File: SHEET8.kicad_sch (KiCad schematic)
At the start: 27 parts, among them J6 CASSETTE, K1 DIP_RELAY, P3 CONN_4, P4 4_PIN_BERG_2X2_STRIP, U1 MC1741, U26 74LS175, U34 8253-5, U63 74LS38, U67 74LS74, U95 75477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

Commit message: Fixed LS and S parts
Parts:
- R10: value 33 -> 33 1/2W
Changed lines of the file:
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@@
 			)
 		)
-		(property "Value" "33"
+		(property "Value" "33 1/2W"
 			(at 316.23 104.14 0)
 			(effects

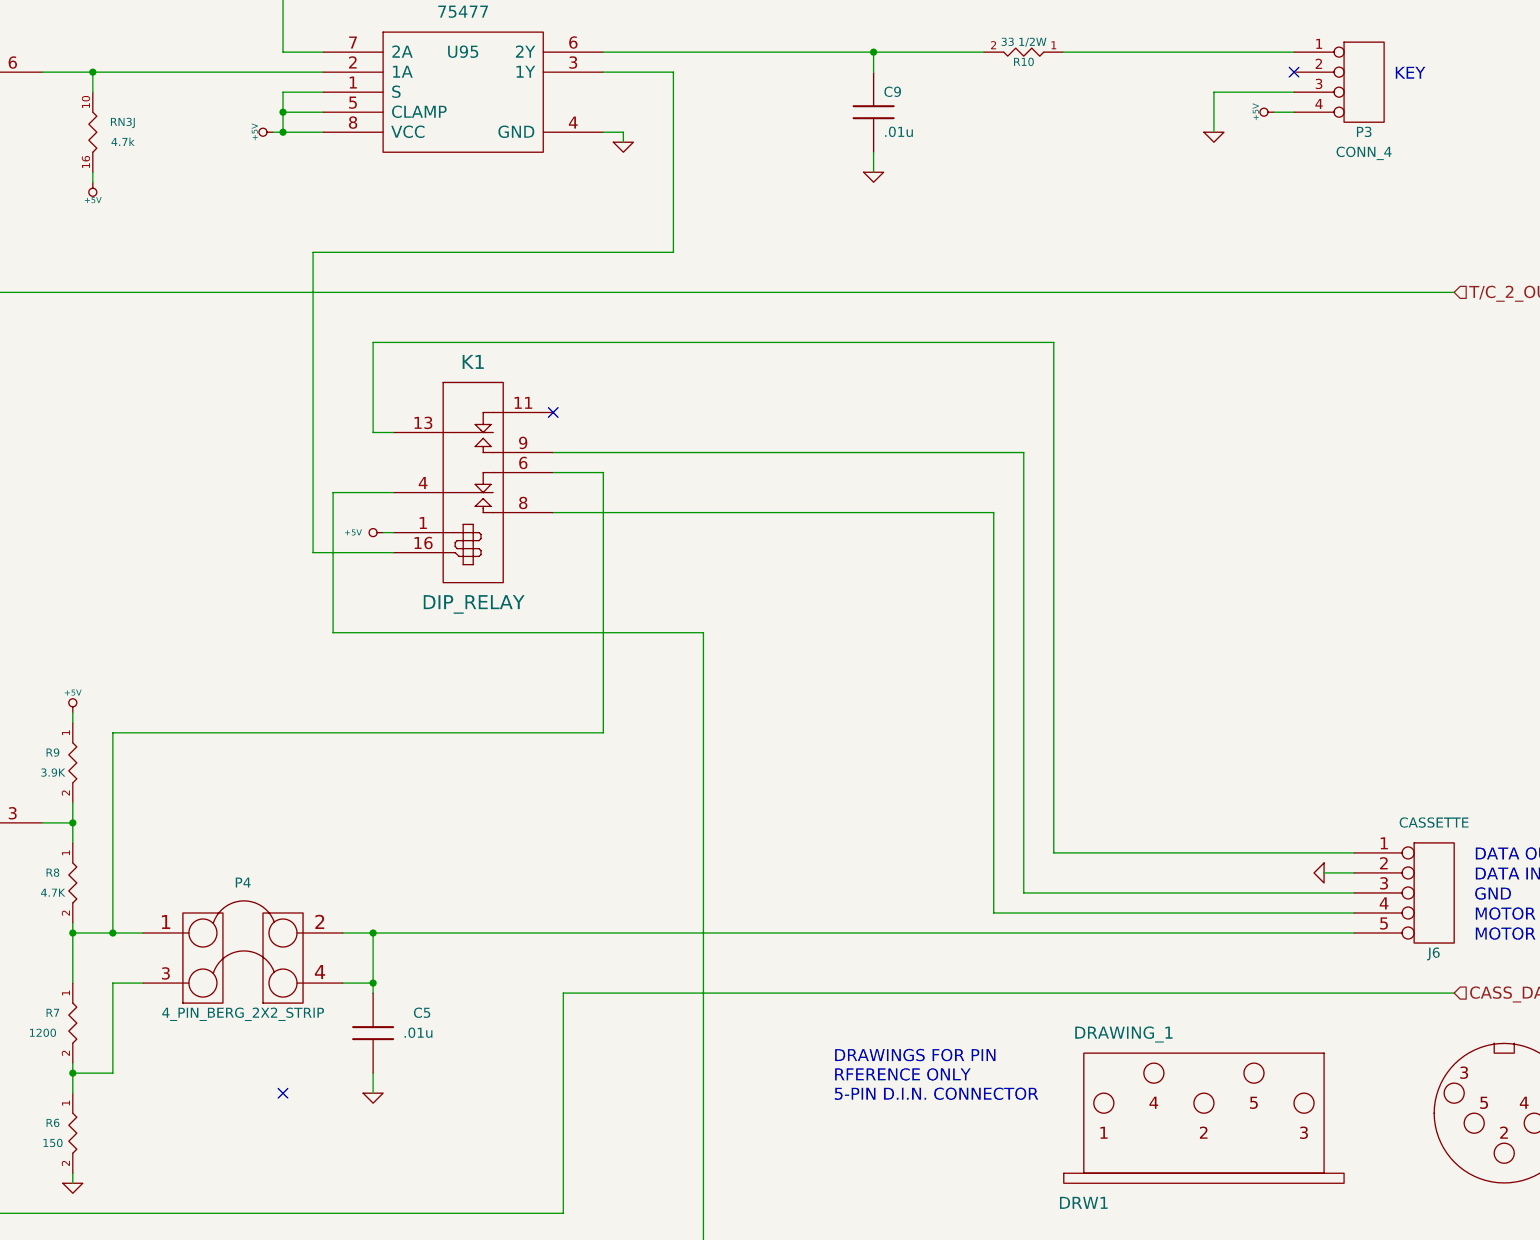
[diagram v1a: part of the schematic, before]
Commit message: added BOM
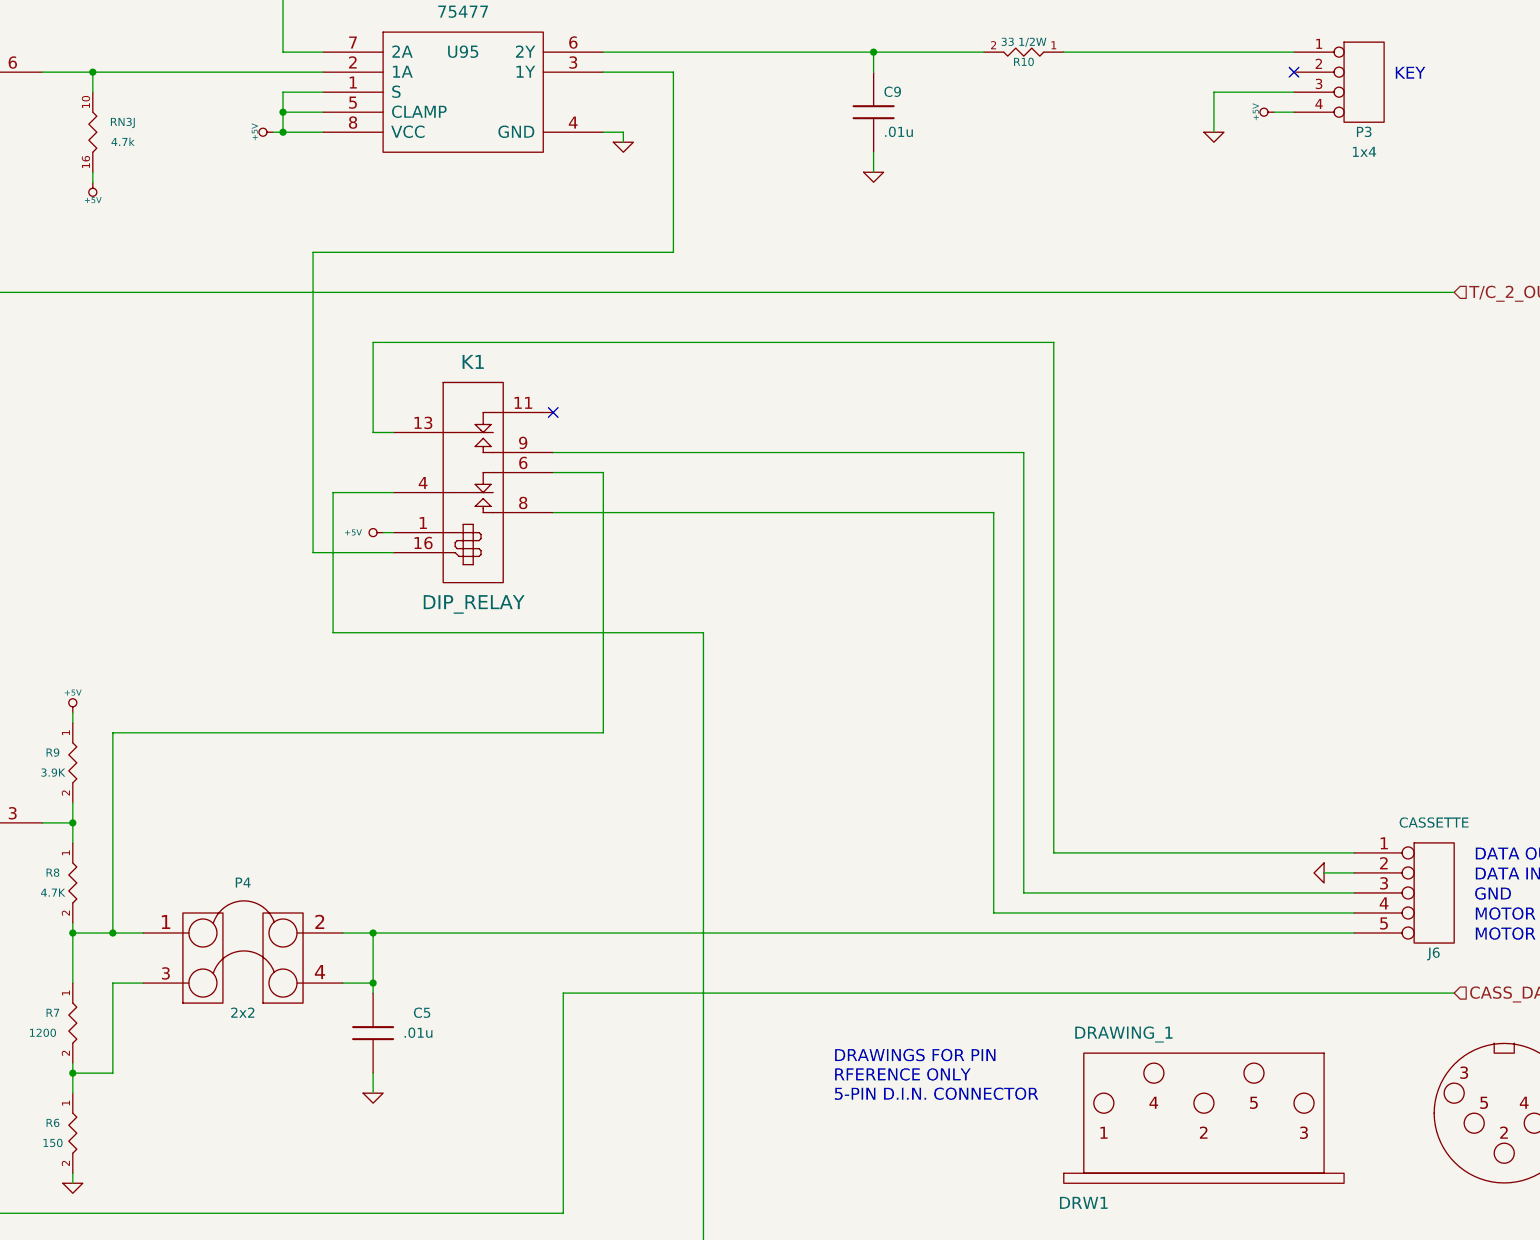
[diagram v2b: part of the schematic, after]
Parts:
- C5, C9: Link (none) -> https://www.digikey.com/en/products/detail/vishay-beyschlag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
- C8: Link (none) -> https://www.digikey.com/en/products/detail/cornell-dubilier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
- D1: Link (none) -> https://www.digikey.com/en/products/detail/onsemi/1N4148/45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
- J6: Link (none) -> https://www.digikey.com/en/products/detail/kycon-inc/KCDX-5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
- K1: Link (none) -> https://www.digikey.com/en/products/detail/omron-electronic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
- P3: value CONN_4 -> 1x4; Link (none) -> https://www.digikey.com/en/products/detail/adam-tech/PH1RB-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
- P4: value 4_PIN_BERG_2X2_STRIP -> 2x2; Link (none) -> https://www.digikey.com/en/products/detail/adam-tech/PH2-04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
- R1, R2, R3, R4, R5, R9: Link (none) -> https://www.digikey.com/en/products/detail/yageo/MFR-25FTE5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
- R10: Link (none) -> https://www.digikey.com/en/products/detail/yageo/MFR50SFTE5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; Note (none) -> 1/2 watt
- R6, R7: Link (none) -> https://www.digikey.com/en/products/detail/yageo/MFR-25FBF5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
- R8: Link (none) -> https://www.digikey.com/en/products/detail/yageo/MFR-25FTF5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
- RN3: Link (none) -> https://www.digikey.com/en/products/detail/bourns-inc/4116R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
- U1, U26, U63, U67, U95, U99: Link (none) -> https://www.digikey.com/en/products/detail/texas-instrument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
- U34: Link (none) -> https://www.jameco.com/z/P8253-Intel-Corporation-Programmab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
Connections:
- no-connect marks 4 -> 3
